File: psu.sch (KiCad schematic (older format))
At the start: 17 parts, among them U7 LM2596S-ADJ, U8 LM2596S-ADJ

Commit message: Several changes.
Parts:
- removed C10, C9: 100nF, Capacitor_SMD:C_1206_3216Metric_Pad1.33x1.80mm_HandSolder, symbol Device:C
- removed JP2: SolderJumper_2_Open, symbol Jumper:SolderJumper_2_Open
- removed L2: 20uH, symbol Device:L
- removed U7, U8: LM2596S-ADJ, Package_TO_SOT_SMD:TO-263-5_TabPin3, symbol Regulator_Switching:LM2596S-ADJ
- added C10A1, C11A1, C12A1, C5A1, C6A1, C8A1, C9A1: ALT, symbol Device:CP
- added C11, C12, C5, C9: 470uF, symbol Device:CP
- added D7A1: ALT, Diode_THT:D_DO-201_P12.70mm_Horizontal, symbol Diode:1N5822
- added L1A1: ALT, symbol Device:L
- added U7: LM2596S-3.3, Package_TO_SOT_SMD:TO-263-5_TabPin3, symbol Regulator_Switching:LM2596S-3.3
- added U7A1: ALT, Package_TO_SOT_THT:TO-220-5_Vertical, symbol Regulator_Switching:LM2596S-3.3
- added U9: LM7805, symbol Regulator_Linear:L7805
- C10: renamed from C7; value 220uF -> 470uF
- C6: renamed from C5; value 680uF -> 470uF
- C8: value 100uF -> 470uF; Fitted (none) -> No; Voltage 16V -> 25V
- L1: value 47uH -> 68uH
- R16: value 100 -> 1k
- R17: renamed from R15; Fitted (none) -> No
- RV1: Fitted (none) -> No
- renumbered C6 to C7, D5 to D6, D4 to D7
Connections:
- net GND: now also C10A1.2, C11.2, C11A1.2, C12.2, C12A1.2, C5.2, C5A1.2, C6A1.2, C8A1.2, C9.2, C9A1.2, D7A1.2 (A), U7.3 (GND), U7.5 (~ON~/OFF), U7A1.3 (GND), U7A1.5 (~ON~/OFF), U9.2 (GND)
- net VIN: now also C8.1, D6.2 (A), C5.1, C5A1.1, C6A1.1, C8A1.1, U7.1 (VIN), U7A1.1 (VIN), U9.1 (IN)
- net VOUT: now also C10.1, JP1.1 (A), L1.2, RV1.1, C10A1.1, C11.1, C11A1.1, C12.1, C12A1.1, L1A1.2; no longer C8.1, D6.2 (A)
- net at D7.1 (K), L1.1: now also D7A1.1 (K), L1A1.1, U7.2 (OUT), U7A1.2 (OUT)
- net at JP1.2 (B), RV1.2: now also U7.4 (FB), U7A1.4 (FB)
- new net VOUT_5V: C9.1, C9A1.1, U9.3 (OUT)
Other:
- note added: "*Duplicated for dual footprints."
- note added: "*Extra power rail for some sensors. Not needed."
- note added: "*Recommended. Not needed."
- note added: "*Recommended. \nNot needed."
- note added: "For 3.3V Version:\n- Solder JP1"
- note added: "For 5.0V/12V\n- Solder RV1\n- Adjust until 3.3v\n- Solder remaining components."
- note added: "For ADJ Version:\n- Solder R17\n- Solder RV1\n- Adjust until 3.3v\n- Solder remaining components."
- note removed: "*Solder JP2 when not in use."
- note removed: "For -3.3V Version:\n- Solder JP1"
- note removed: "For -5.0V or -12V\n- Solder RV1\n- Adjust until 3.3v"
- note removed: "For -ADJ Version:\n- Solder R15\n- Solder RV1\n- Adjust until 3.3v"
- note removed: "Optional Output\nRipple Filter"
- moved on the sheet: C10, C6, C7, D6, D7, JP1, L1, R16, R17, RV1

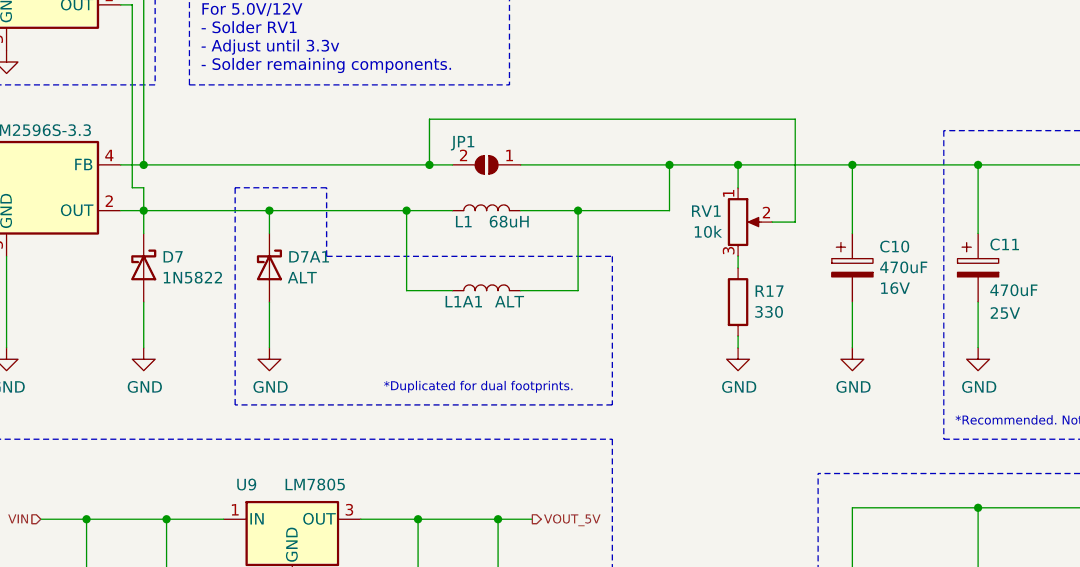
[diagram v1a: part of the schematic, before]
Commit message: Full update to psu.sch
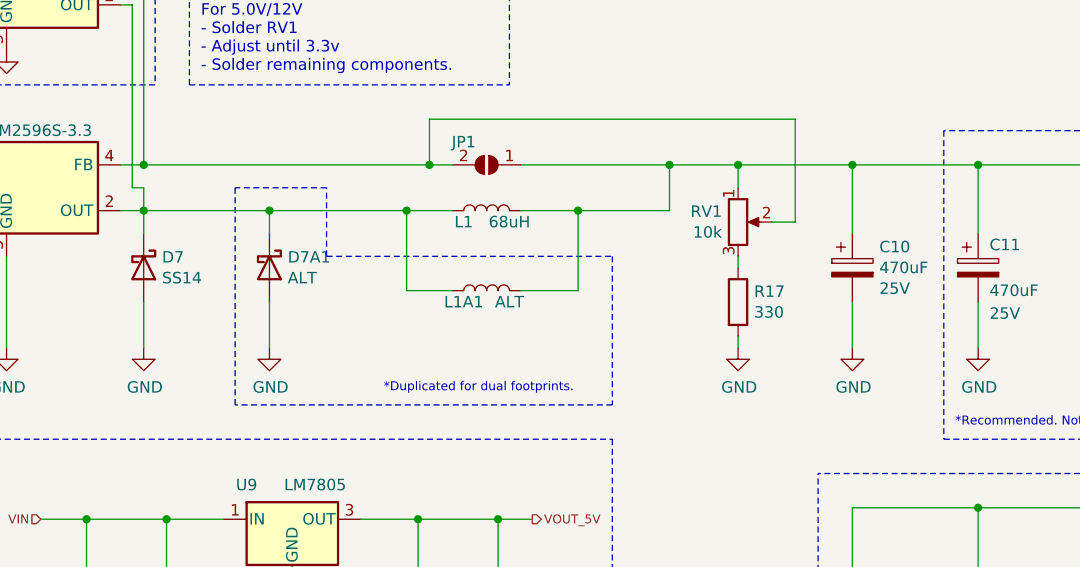
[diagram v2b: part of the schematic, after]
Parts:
- C10: footprint (none) -> Capacitor_SMD:CP_Elec_10x10; Voltage 16V -> 25V; manf# (none) -> EEE-1EA471UAP
- C10A1, C11A1, C12A1, C5A1, C6A1: footprint (none) -> Capacitor_THT:CP_Radial_D10.0mm_P3.80mm; Fitted (none) -> No; Voltage (none) -> 25V; manf# (none) -> UHE1E471MPD6
- C11, C12, C5, C6, C8, C9: footprint (none) -> Capacitor_SMD:CP_Elec_10x10; manf# (none) -> EEE-1EA471UAP
- C7: Voltage (none) -> 50V; manf# (none) -> CC1206KRX7R9BB104
- C8A1, C9A1: footprint (none) -> Capacitor_THT:CP_Radial_D10.0mm_P3.80mm; Voltage (none) -> 25V; manf# (none) -> UHE1E471MPD6
- D6: footprint (none) -> LED_SMD:LED_1206_3216Metric; manf# (none) -> BR1101W-TR
- D7: value 1N5822 -> SS14; footprint Diode_THT:D_DO-201_P12.70mm_Horizontal -> Diode_SMD:D_SMA_Handsoldering; manf# (none) -> SS14
- D7A1: Fitted (none) -> No; manf# (none) -> 1N5819
- L1: footprint (none) -> Inductor_SMD:L_12x12mm_H8mm; manf# (none) -> P0751.683NLT, CDRH127/LDNP-680MC
- L1A1: footprint (none) -> Inductor_THT:L_Radial_D12.0mm_P5.00mm_Fastron_11P; Fitted (none) -> No; manf# (none) -> RLB0914-680KL
- R16: footprint (none) -> Resistor_SMD:R_1206_3216Metric; manf# (none) -> RC1206FR-071KL
- R17: footprint (none) -> Resistor_SMD:R_1206_3216Metric; manf# (none) -> RC1206FR-07330RL
- RV1: manf# (none) -> 3296W-1-103RLF
- U7: manf# (none) -> LM2596SX-3.3/NOPB
- U7A1: Fitted (none) -> No; manf# (none) -> LM2596T-3.3/LF03
- U9: footprint (none) -> Package_TO_SOT_THT:TO-220-3_Vertical; manf# (none) -> LM7805CT/NOPB

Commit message: various updates
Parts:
- JP1: footprint (none) -> Jumper:SolderJumper-2_P1.3mm_Open_RoundedPad1.0x1.5mm
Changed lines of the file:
@@
 F 0 "JP1" H 6800 3200 50  0000 C CNN
 F 1 "SolderJumper_2_Open" V 6745 3368 50  0001 L CNN
-F 2 "" H 6700 3300 50  0001 C CNN
+F 2 "Jumper:SolderJumper-2_P1.3mm_Open_RoundedPad1.0x1.5mm" H 6700 3300 50  0001 C CNN
 F 3 "~" H 6700 3300 50  0001 C CNN
 	1    6700 3300
